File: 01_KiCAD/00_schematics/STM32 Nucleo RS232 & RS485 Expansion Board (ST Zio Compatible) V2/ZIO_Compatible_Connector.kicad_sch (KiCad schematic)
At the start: 4 parts, among them CN10 Conn_02x17_Odd_Even, CN7 Conn_02x10_Odd_Even, CN8 Conn_02x08_Odd_Even, CN9 Conn_02x15_Odd_Even

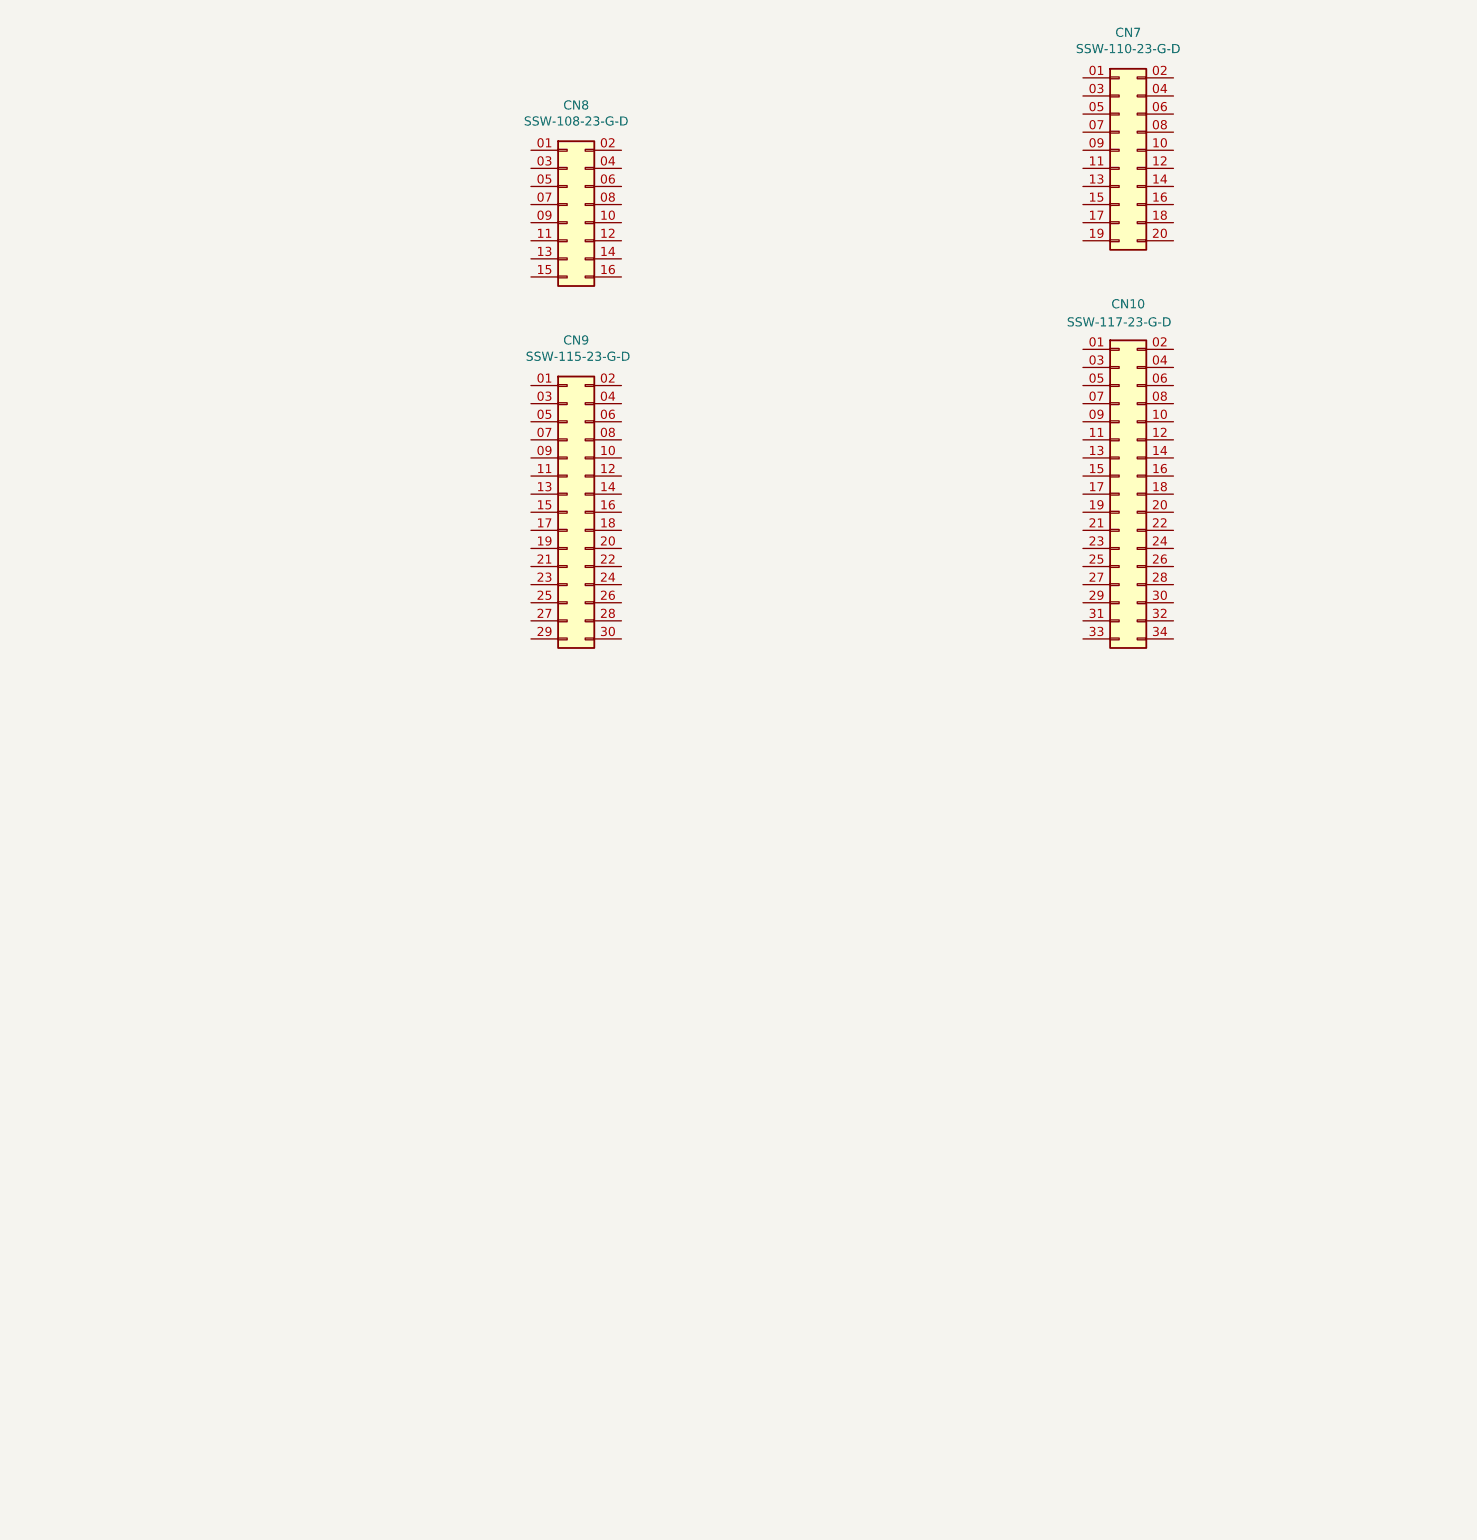
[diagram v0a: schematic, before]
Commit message: Added SHDN logic
Added the SHDN pin logic to have both hardware control and software control vor activating the THVD4431
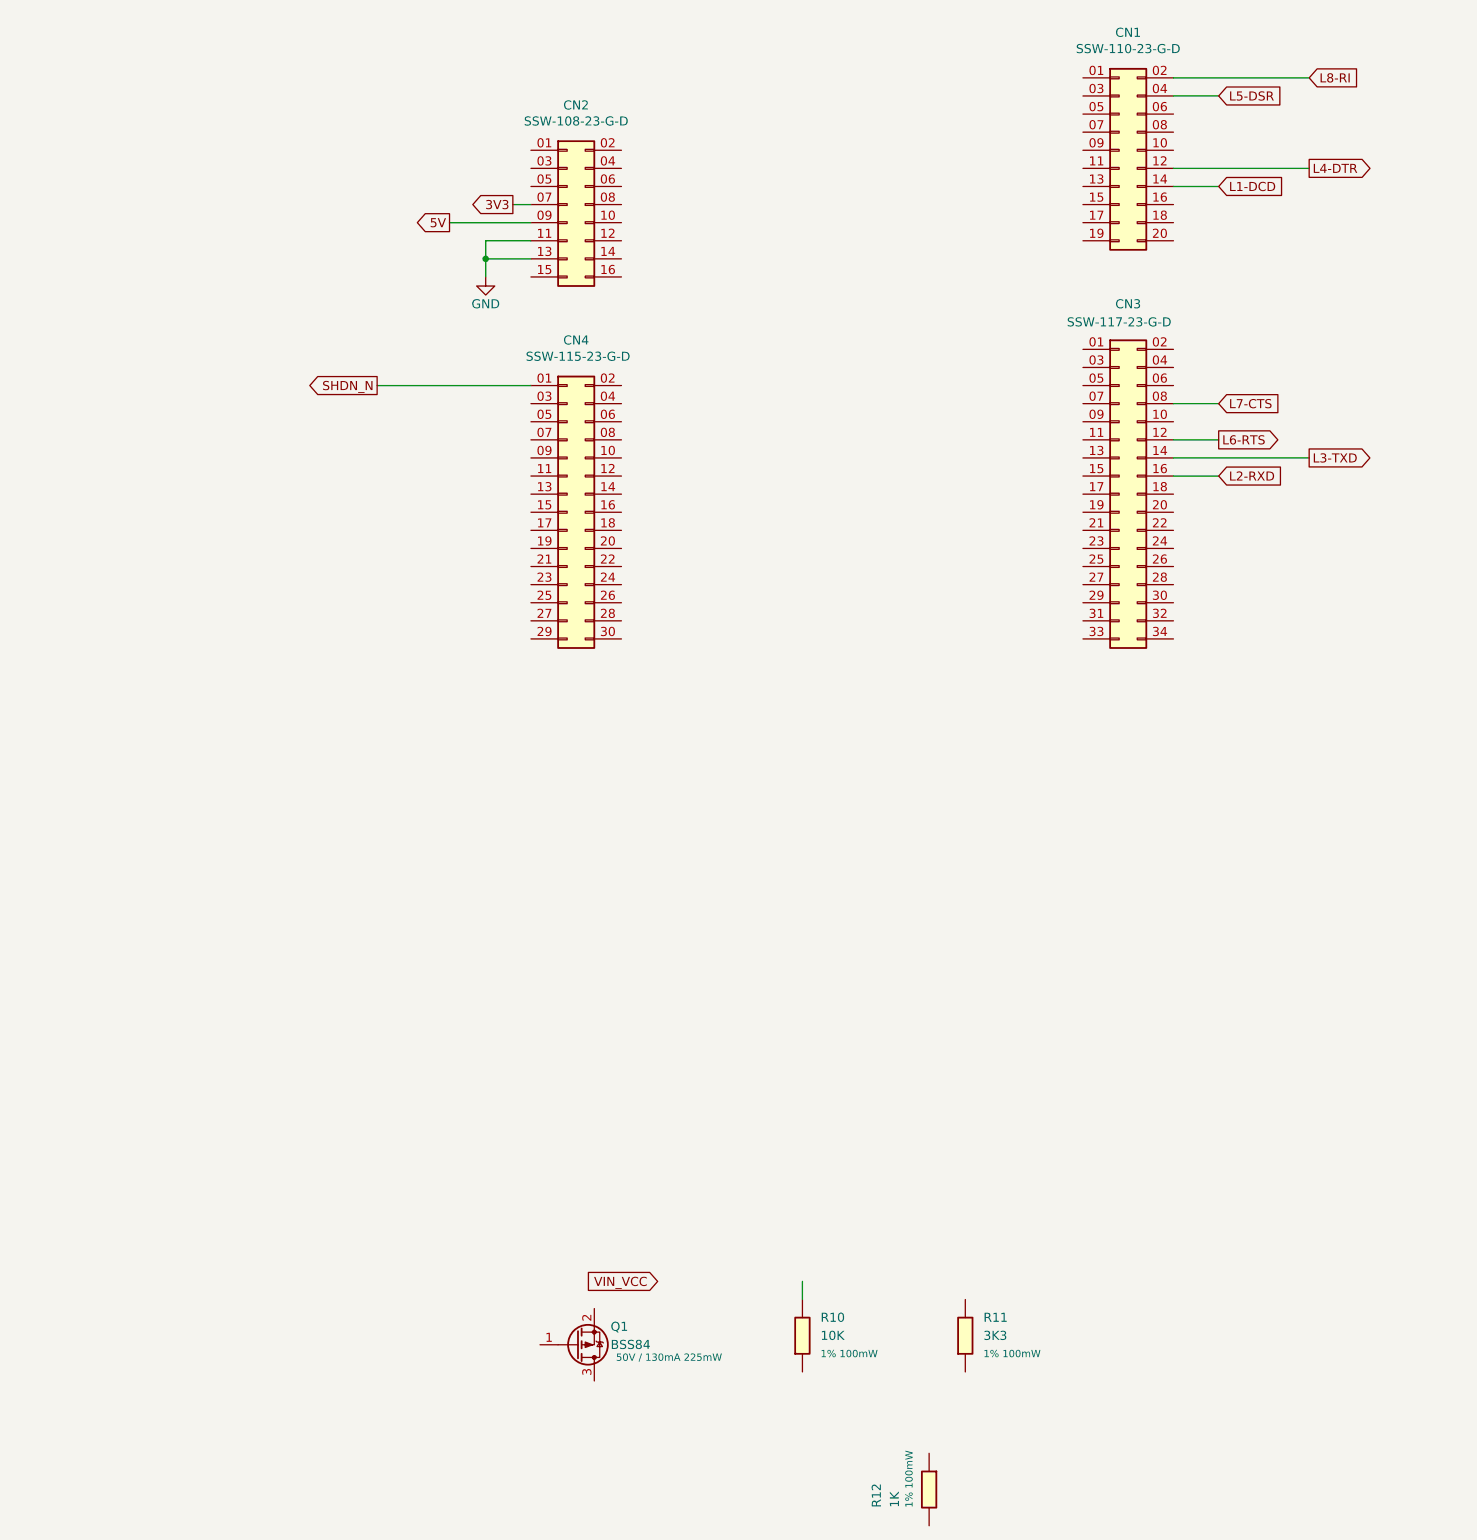
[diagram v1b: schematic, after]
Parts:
- added Q1: BSS84, Package_TO_SOT_SMD:SOT-23, symbol Transistor_FET:BSS84
- added R10: 10K, PCM_fab:R_0603, symbol PCM_fab:R_0603
- added R11: 3K3, PCM_fab:R_0603, symbol PCM_fab:R_0603
- added R12: 1K, PCM_fab:R_0603, symbol PCM_fab:R_0603
- renumbered CN7 to CN1, CN8 to CN2, CN10 to CN3, CN9 to CN4
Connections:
- net SHDN_N: now reaches CN4.01 (Pin_1)
- net L8-RI: now reaches CN1.02 (Pin_2)
- net L5-DSR: now reaches CN1.04 (Pin_4)
- net L4-DTR: now reaches CN1.12 (Pin_12)
- net L1-DCD: now reaches CN1.14 (Pin_14)
- net 3V3: now reaches CN2.07 (Pin_7)
- net 5V: now reaches CN2.09 (Pin_9)
- net GND: now reaches CN2.11 (Pin_11)
- net GND: now also CN2.13 (Pin_13)
- net L7-CTS: now reaches CN3.08 (Pin_8)
- net L6-RTS: now reaches CN3.12 (Pin_12)
- net L3-TXD: now reaches CN3.14 (Pin_14)
- net L2-RXD: now reaches CN3.16 (Pin_16)

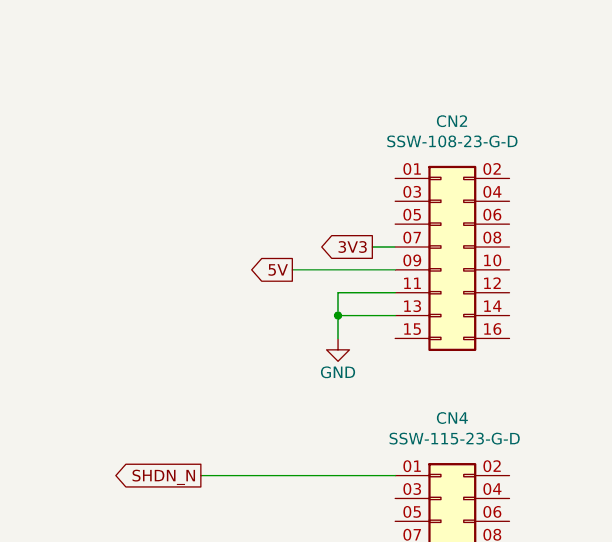
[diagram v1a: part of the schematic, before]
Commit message: Added Dual Voltage Input
Added Dual Voltage Auto Select Input drawings. Added new hierarchical sheet with new pagenumber one. All other pages have been moved up by 1.
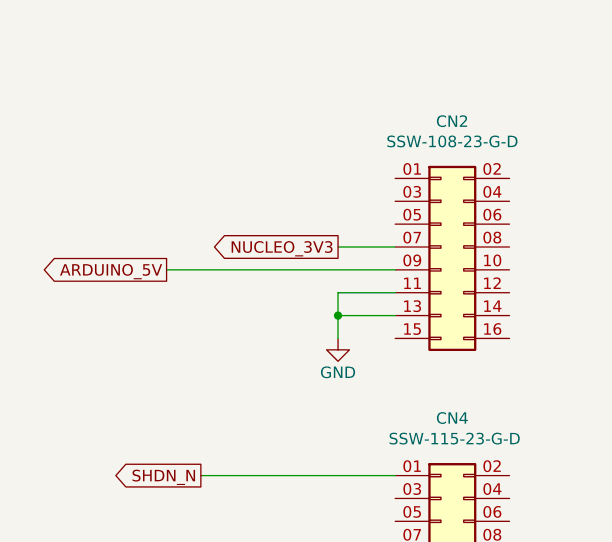
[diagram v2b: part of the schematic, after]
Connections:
- net 3V3 renamed NUCLEO_3V3
- net 5V renamed ARDUINO_5V
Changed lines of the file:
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@@
 	(wire
 		(pts
-			(xy 87.63 74.93) (xy 99.06 74.93)
+			(xy 73.66 74.93) (xy 99.06 74.93)
 		)
 		(stroke
@@
 	(wire
 		(pts
-			(xy 96.52 72.39) (xy 99.06 72.39)
+			(xy 92.71 72.39) (xy 99.06 72.39)
 		)
 		(stroke
@@
 		)
 	)
-	(global_label "3V3"
-		(shape output)
-		(at 96.52 72.39 180)
+	(global_label "NUCLEO_3V3"
+		(shape output)
+		(at 92.71 72.39 180)
 		(fields_autoplaced yes)
 		(effects
@@
 		)
 		(property "Intersheetrefs" "${INTERSHEET_REFS}"
-			(at 90.0272 72.39 0)
+			(at 77.811 72.39 0)
 			(effects
 				(font
@@
 		)
 	)
-	(global_label "5V"
-		(shape output)
-		(at 87.63 74.93 180)
+	(global_label "ARDUINO_5V"
+		(shape output)
+		(at 73.66 74.93 180)
 		(fields_autoplaced yes)
 		(effects
@@
 		)
 		(property "Intersheetrefs" "${INTERSHEET_REFS}"
-			(at 82.3467 74.93 0)
-			(effects
-				(font
+			(at 59.1842 74.93 0)
+			(effects
+				(font
